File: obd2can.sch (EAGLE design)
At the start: 83 parts, among them IC1 LM339PWR, IC2 SCANTOOL, Q1 BSS138, Q2 MMBT2222, Q3 ZXMP6A13FTA, Q4 BSS138, Q5 MMBT2222, Q6 MMBT2222, Q7 8MHz, SW1 6X3.5_TACT, U1 V_REG_317SMD, U2 SN65HVD235DR, U3 MCP1700-5.0, U4 STM32F072-LQFP48, U8 MCP1700-3.3, X1 RJ45_RIGHT_ANGLEMOLEX_95001-2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, X2 RJ45_RIGHT_ANGLEMOLEX_95001-2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, Y1 16MHz

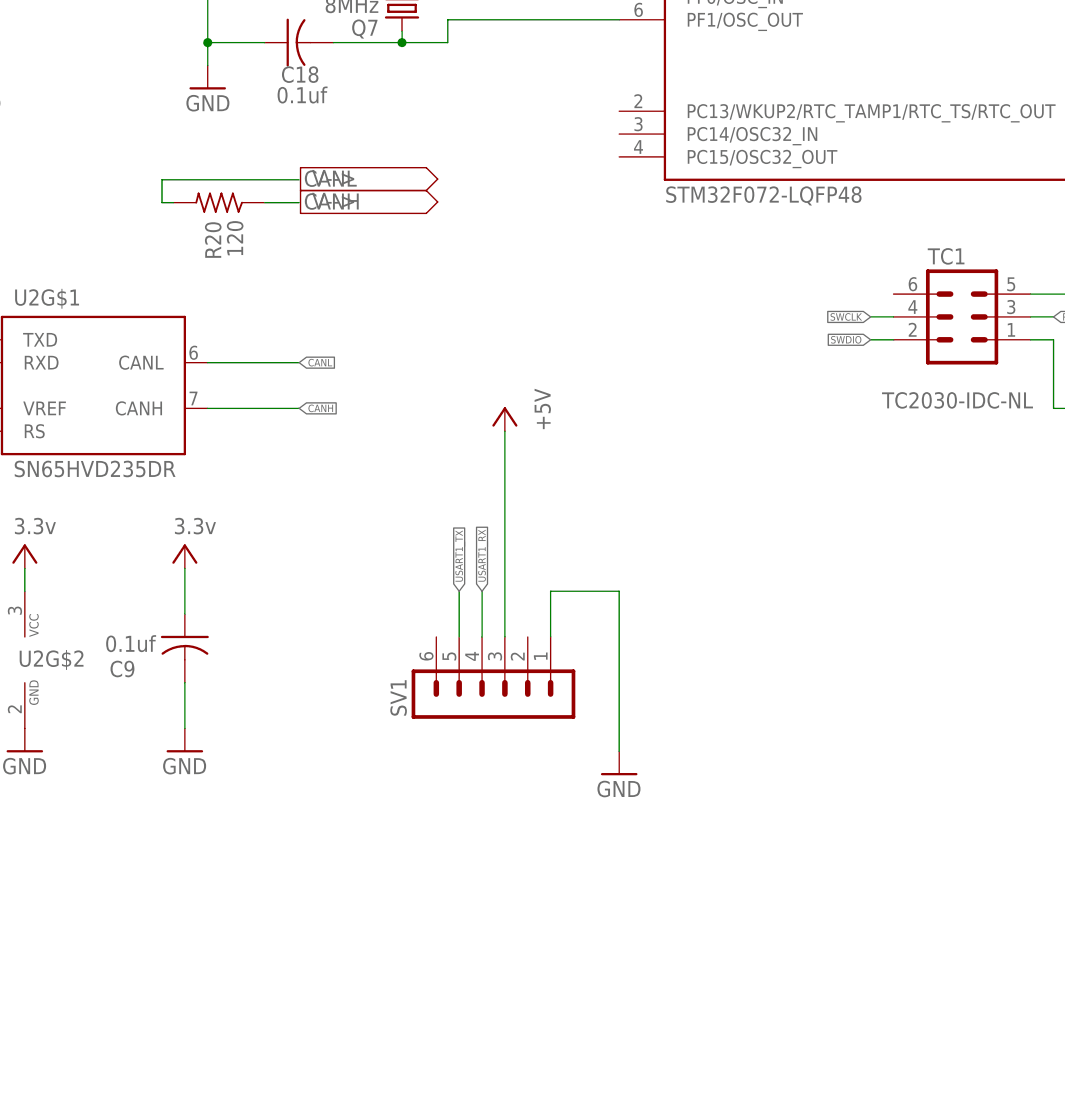
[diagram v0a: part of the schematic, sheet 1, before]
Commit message: added the ability to supply power via FTDI header
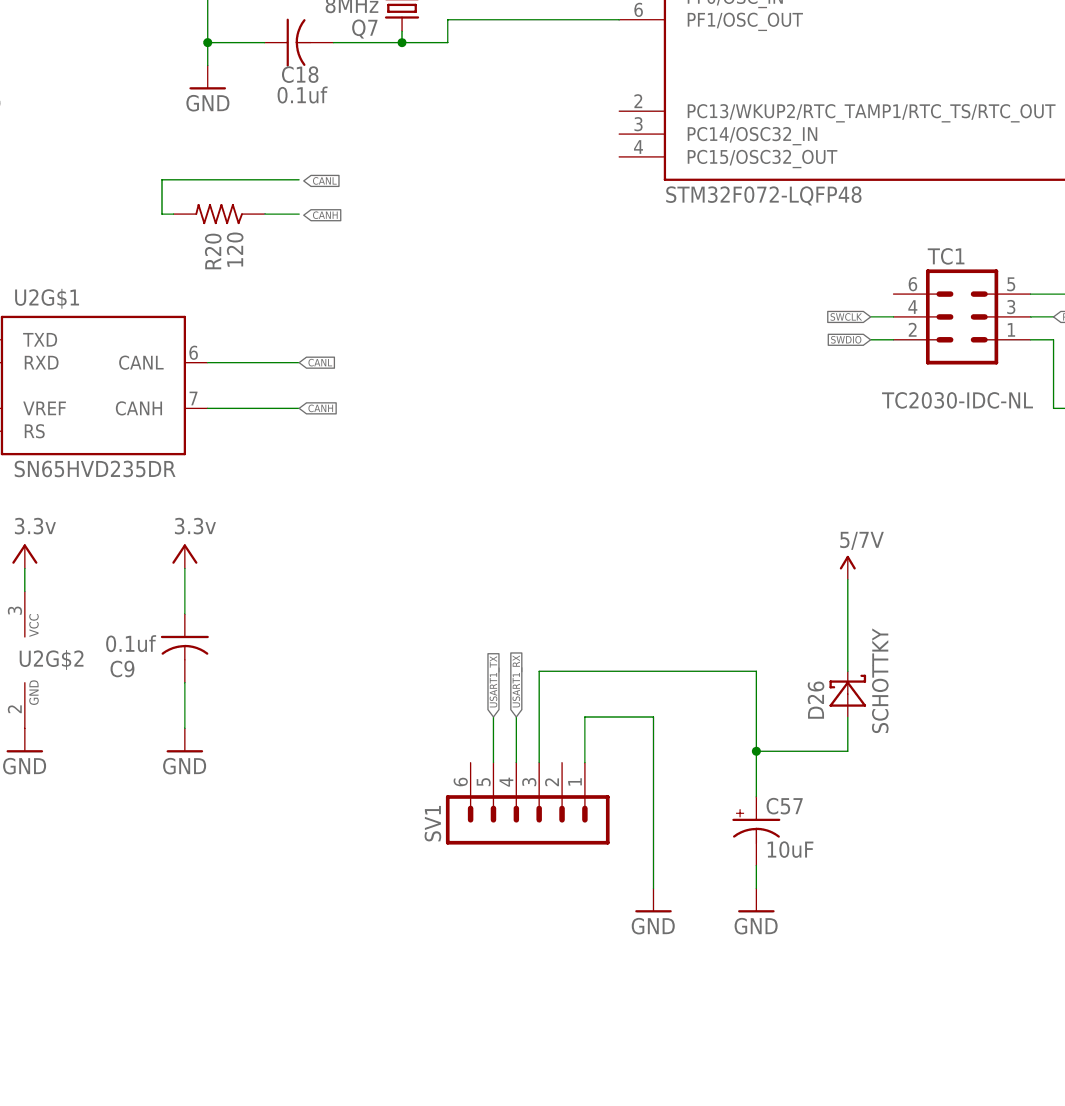
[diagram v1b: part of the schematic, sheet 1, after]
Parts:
- added C57: 10uF, rcl:CPOL-USSMCA
- added D26: SCHOTTKY, smt_diodes:SCHOTTKY
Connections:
- removed net +5V: SV1.3
- new net VBUS: C57.+, D26.A, SV1.3
- net GND: now also C57.-
- net VCC: now also D26.C
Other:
- note added: "STN Controller"
- note removed: "Main Controller"
- moved on the sheet: C4, R20, SV1

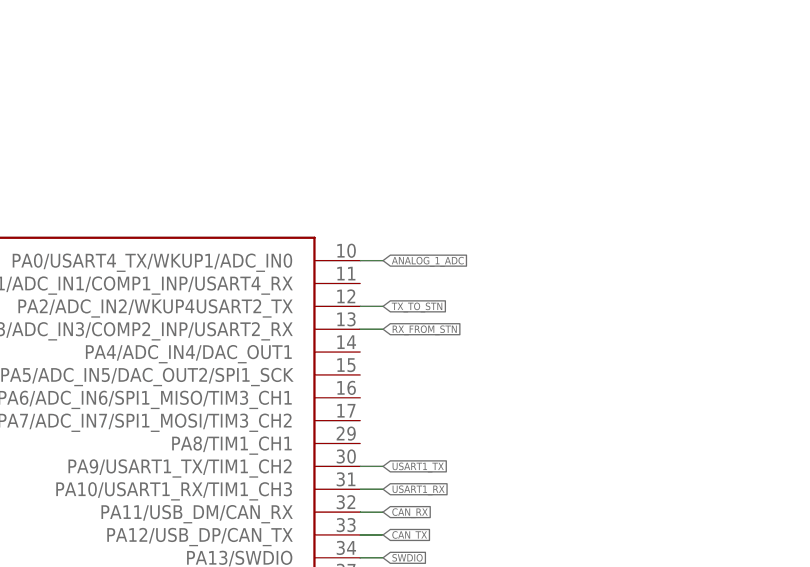
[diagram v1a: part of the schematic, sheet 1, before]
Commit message: add NVM_RST line between STM32 and STN chips
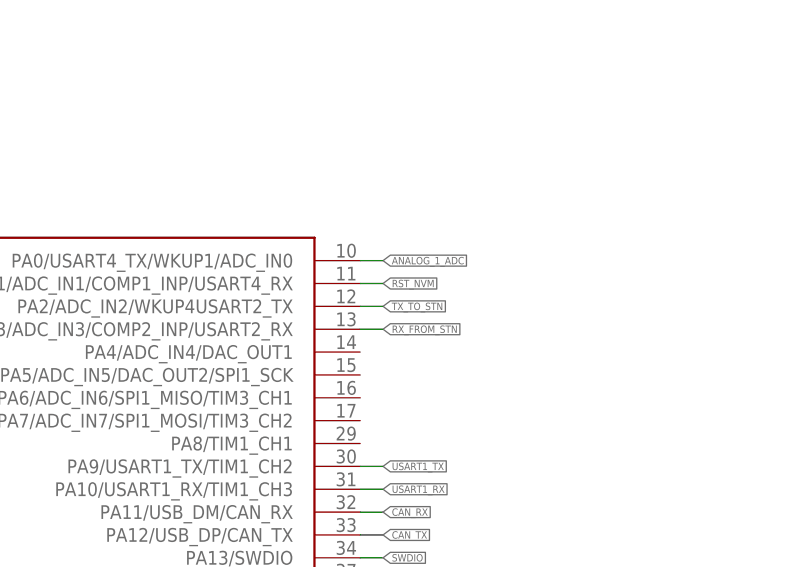
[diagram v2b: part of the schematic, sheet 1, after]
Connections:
- net RST_NVM: now also U4.PA1/ADC_IN1/COMP1_INP/USART4_RX
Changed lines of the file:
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@@
 <setting verticaltext="up"/>
 </settings>
-<grid distance="0.05" unitdist="inch" unit="inch" style="lines" multiple="1" display="no" altdistance="0.01" altunitdist="inch" altunit="inch"/>
+<grid distance="0.1" unitdist="inch" unit="inch" style="lines" multiple="1" display="yes" altdistance="0.01" altunitdist="inch" altunit="inch"/>
 <layers>
 <layer number="1" name="Top" color="4" fill="1" visible="no" active="no"/>
@@
 </segment>
 </net>
+<net name="RST_NVM" class="0">
+<segment>
+<pinref part="U4" gate="G$1" pin="PA1/ADC_IN1/COMP1_INP/USART4_RX"/>
+<wire x1="716.28" y1="167.64" x2="718.82" y2="167.64" width="0.1524" layer="91"/>
+<label x="718.82" y="167.64" size="0.8128" layer="95" xref="yes"/>
+</segment>
+</net>
 </nets>
 </sheet>
@@
 <wire x1="337.82" y1="213.36" x2="337.82" y2="218.44" width="0.1524" layer="91"/>
 <junction x="337.82" y="213.36"/>
-<label x="350.52" y="213.36" size="1.778" layer="95"/>
 <pinref part="IC2" gate="G$1" pin="!OBD_TX_LED!/!RST_NVM"/>
 <pinref part="R11" gate="G$1" pin="2"/>
+<label x="363.22" y="213.36" size="1.778" layer="95" ratio="6" xref="yes"/>
 </segment>
 </net>
